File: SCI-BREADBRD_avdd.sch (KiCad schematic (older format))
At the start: 25 parts, among them P8 AVDD, U2 TPS62240DDC, U3 TPS73401DDC, U4 TS5A3159ADCK, U5 TS5A3159ADCK

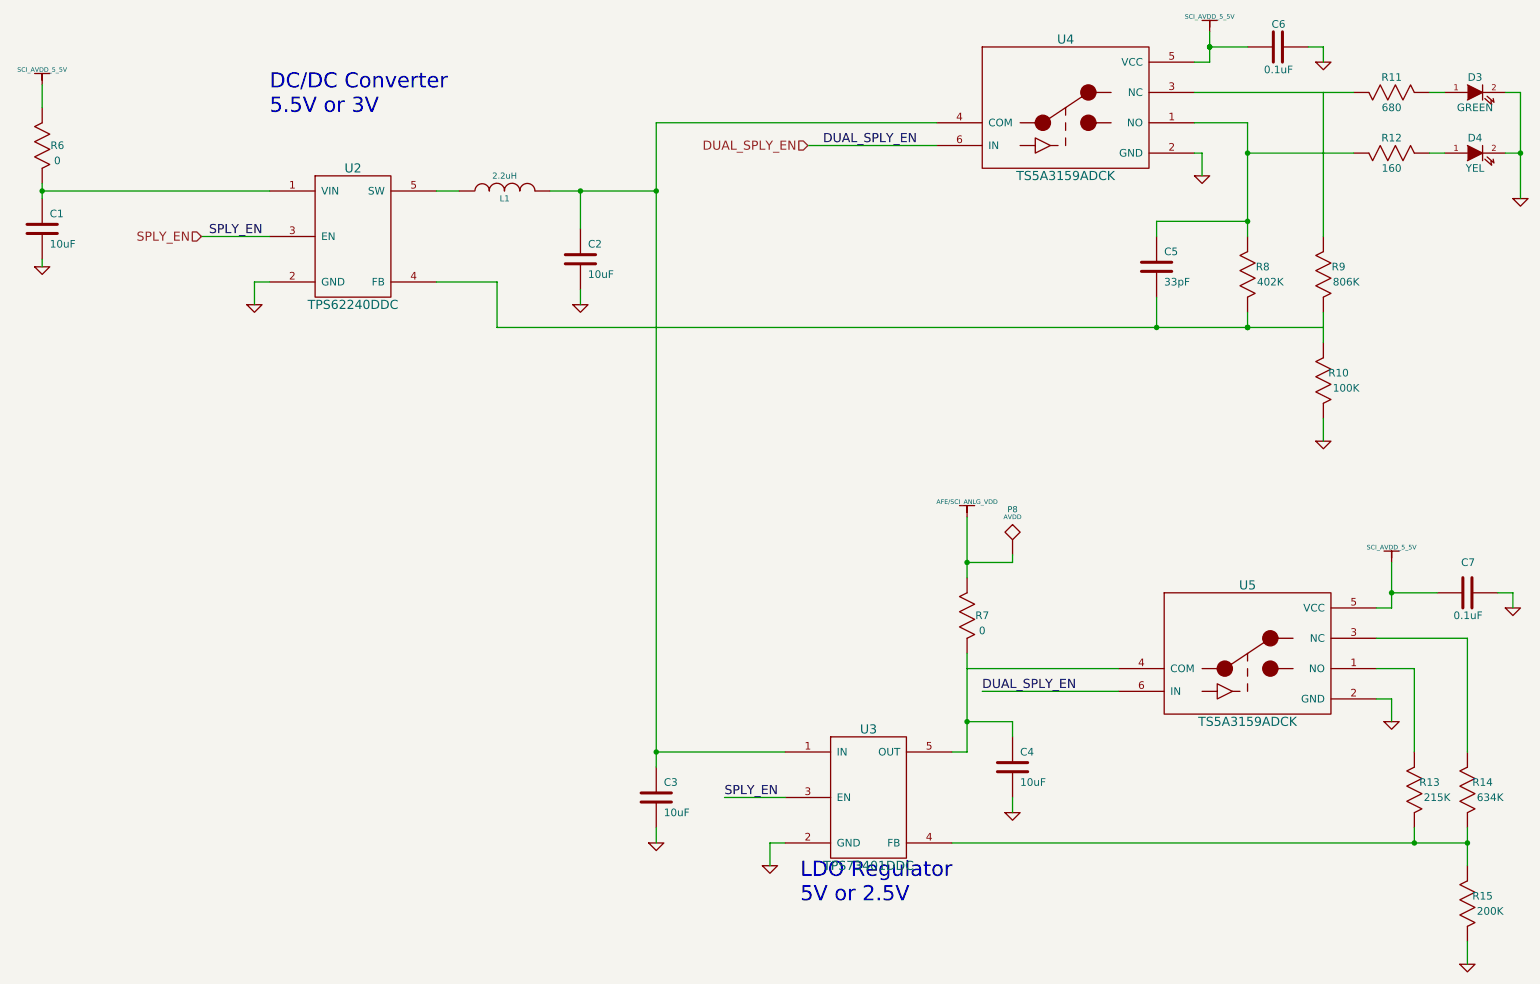
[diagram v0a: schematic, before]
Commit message: Completed ERC. Added some power flags and fixed mis-connected pins.
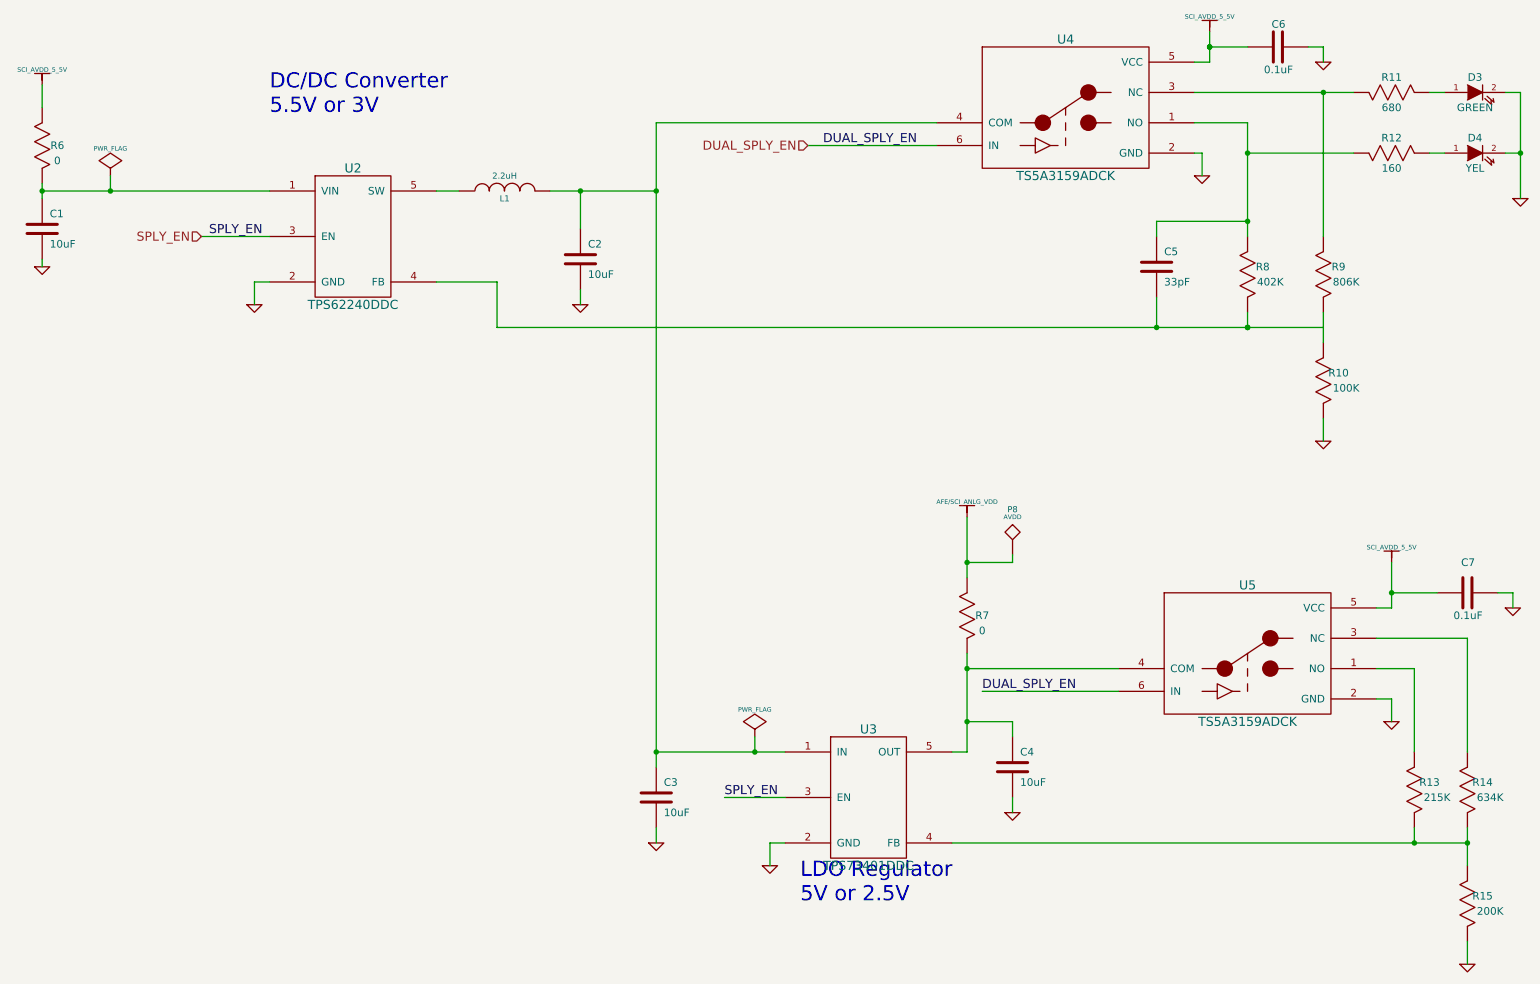
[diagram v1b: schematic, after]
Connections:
- wire segments 70 -> 72
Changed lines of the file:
@@
-EESchema Schematic File Version 2  date Fri 27 Apr 2012 09:11:54 AM EDT
+EESchema Schematic File Version 2  date Fri 27 Apr 2012 11:11:24 AM EDT
 LIBS:custom_transistors
 LIBS:TI_custom
@@
 $EndComp
 $Comp
-L SCI_AVDD_5_5V #PWR046
+L SCI_AVDD_5_5V #PWR050
 U 1 1 4F9A30C2
 P 1000 1150
-F 0 "#PWR046" H 1000 1250 30  0001 C CNN
+F 0 "#PWR050" H 1000 1250 30  0001 C CNN
 F 1 "SCI_AVDD_5_5V" H 1000 1250 30  0000 C CNN
 	1    1000 1150
@@
 $EndComp
 $Comp
-L GND #PWR047
+L GND #PWR051
 U 1 1 4F9A30C8
 P 2400 2600
-F 0 "#PWR047" H 2400 2600 30  0001 C CNN
+F 0 "#PWR051" H 2400 2600 30  0001 C CNN
 F 1 "GND" H 2400 2530 30  0001 C CNN
 	1    2400 2600
@@
 $EndComp
 $Comp
-L GND #PWR048
+L GND #PWR052
 U 1 1 4F9A30D7
 P 1000 2350
-F 0 "#PWR048" H 1000 2350 30  0001 C CNN
+F 0 "#PWR052" H 1000 2350 30  0001 C CNN
 F 1 "GND" H 1000 2280 30  0001 C CNN
 	1    1000 2350
@@
 $EndComp
 $Comp
-L GND #PWR049
+L GND #PWR053
 U 1 1 4F9A30F8
 P 4550 2600
-F 0 "#PWR049" H 4550 2600 30  0001 C CNN
+F 0 "#PWR053" H 4550 2600 30  0001 C CNN
 F 1 "GND" H 4550 2530 30  0001 C CNN
 	1    4550 2600
@@
 $EndComp
 $Comp
-L GND #PWR050
+L GND #PWR054
 U 1 1 4F9A312B
 P 8650 1750
-F 0 "#PWR050" H 8650 1750 30  0001 C CNN
+F 0 "#PWR054" H 8650 1750 30  0001 C CNN
 F 1 "GND" H 8650 1680 30  0001 C CNN
 	1    8650 1750
@@
 $EndComp
 $Comp
-L SCI_AVDD_5_5V #PWR051
+L SCI_AVDD_5_5V #PWR055
 U 1 1 4F9A3131
 P 8700 800
-F 0 "#PWR051" H 8700 900 30  0001 C CNN
+F 0 "#PWR055" H 8700 900 30  0001 C CNN
 F 1 "SCI_AVDD_5_5V" H 8700 900 30  0000 C CNN
 	1    8700 800
@@
 $EndComp
 $Comp
-L GND #PWR052
+L GND #PWR056
 U 1 1 4F9A3140
 P 5800 6300
-F 0 "#PWR052" H 5800 6300 30  0001 C CNN
+F 0 "#PWR056" H 5800 6300 30  0001 C CNN
 F 1 "GND" H 5800 6230 30  0001 C CNN
 	1    5800 6300
@@
 $EndComp
 $Comp
-L SCI_AVDD_5_5V #PWR053
+L SCI_AVDD_5_5V #PWR057
 U 1 1 4F9A3161
 P 9900 4300
-F 0 "#PWR053" H 9900 4400 30  0001 C CNN
+F 0 "#PWR057" H 9900 4400 30  0001 C CNN
 F 1 "SCI_AVDD_5_5V" H 9900 4400 30  0000 C CNN
 	1    9900 4300
@@
 $EndComp
 $Comp
-L GND #PWR054
+L GND #PWR058
 U 1 1 4F9A3167
 P 9900 5350
-F 0 "#PWR054" H 9900 5350 30  0001 C CNN
+F 0 "#PWR058" H 9900 5350 30  0001 C CNN
 F 1 "GND" H 9900 5280 30  0001 C CNN
 	1    9900 5350
@@
 $EndComp
 $Comp
-L GND #PWR055
+L GND #PWR059
 U 1 1 4F9A316D
 P 10400 6950
-F 0 "#PWR055" H 10400 6950 30  0001 C CNN
+F 0 "#PWR059" H 10400 6950 30  0001 C CNN
 F 1 "GND" H 10400 6880 30  0001 C CNN
 	1    10400 6950
@@
 $EndComp
 $Comp
-L GND #PWR056
+L GND #PWR060
 U 1 1 4F9A3173
 P 9450 3500
-F 0 "#PWR056" H 9450 3500 30  0001 C CNN
+F 0 "#PWR060" H 9450 3500 30  0001 C CNN
 F 1 "GND" H 9450 3430 30  0001 C CNN
 	1    9450 3500
@@
 $EndComp
 $Comp
-L GND #PWR057
+L GND #PWR061
 U 1 1 4F9A318D
 P 7400 5950
-F 0 "#PWR057" H 7400 5950 30  0001 C CNN
+F 0 "#PWR061" H 7400 5950 30  0001 C CNN
 F 1 "GND" H 7400 5880 30  0001 C CNN
 	1    7400 5950
@@
 $EndComp
 $Comp
-L GND #PWR058
+L GND #PWR062
 U 1 1 4F9A319C
 P 5050 6150
-F 0 "#PWR058" H 5050 6150 30  0001 C CNN
+F 0 "#PWR062" H 5050 6150 30  0001 C CNN
 F 1 "GND" H 5050 6080 30  0001 C CNN
 	1    5050 6150
@@
 $EndComp
 $Comp
-L AFE/SCI_ANLG_VDD #PWR059
+L AFE/SCI_ANLG_VDD #PWR063
 U 1 1 4F9A31AB
 P 7100 4000
-F 0 "#PWR059" H 7100 4100 30  0001 C CNN
+F 0 "#PWR063" H 7100 4100 30  0001 C CNN
 F 1 "AFE/SCI_ANLG_VDD" H 7100 4100 30  0000 C CNN
 	1    7100 4000
@@
 $EndComp
 $Comp
-L GND #PWR060
+L GND #PWR064
 U 1 1 4F9A5608
 P 10750 1900
-F 0 "#PWR060" H 10750 1900 30  0001 C CNN
+F 0 "#PWR064" H 10750 1900 30  0001 C CNN
 F 1 "GND" H 10750 1830 30  0001 C CNN
 	1    10750 1900
@@
 $EndComp
 $Comp
-L GND #PWR061
+L GND #PWR065
 U 1 1 4F9A573A
 P 10700 4600
-F 0 "#PWR061" H 10700 4600 30  0001 C CNN
+F 0 "#PWR065" H 10700 4600 30  0001 C CNN
 F 1 "GND" H 10700 4530 30  0001 C CNN
 	1    10700 4600
@@
 $EndComp
 $Comp
-L GND #PWR062
+L GND #PWR066
 U 1 1 4F9A5AE1
 P 9450 1000
-F 0 "#PWR062" H 9450 1000 30  0001 C CNN
+F 0 "#PWR066" H 9450 1000 30  0001 C CNN
 F 1 "GND" H 9450 930 30  0001 C CNN
 	1    9450 1000
 	1    0    0    -1
 $EndComp
+$Comp
+L PWR_FLAG #FLG067
+U 1 1 4F9AE62C
+P 5700 5450
+F 0 "#FLG067" H 5700 5545 30  0001 C CNN
+F 1 "PWR_FLAG" H 5700 5630 30  0000 C CNN
+	1    5700 5450
+	1    0    0    -1
+$EndComp
+$Comp
+L PWR_FLAG #FLG068
+U 1 1 4F9AE6F0
+P 1450 1750
+F 0 "#FLG068" H 1450 1845 30  0001 C CNN
+F 1 "PWR_FLAG" H 1450 1930 30  0000 C CNN
+	1    1450 1750
+	1    0    0    -1
+$EndComp
 Wire Wire Line
 	1000 1150 1000 1300
@@
 Wire Wire Line
 	8600 1200 9650 1200
-Wire Wire Line
-	9450 1200 9450 2150
 Wire Wire Line
 	9450 2650 9450 2850
@@
 	7100 4900 7100 5550
 Wire Wire Line
-	7100 5000 8100 5000
-Wire Wire Line
 	9900 5200 9800 5200
 Wire Wire Line
@@
 Wire Wire Line
 	9450 900  9450 1000
+Wire Wire Line
+	9450 2150 9450 1200
+Connection ~ 9450 1200
+Wire Wire Line
+	8100 5000 7100 5000
+Connection ~ 7100 5000
+Wire Wire Line
+	5700 5450 5700 5550
+Connection ~ 5700 5550
+Wire Wire Line
+	1450 1750 1450 1850
+Connection ~ 1450 1850
 $EndSCHEMATC

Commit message: Changed the testpoints to have a refdes of TP? instead of P? and re-annotated.
Fixed a but in better_bom that was causing the last field to be
erroneous.

Added the -e option to better_bom to allow excluding fields
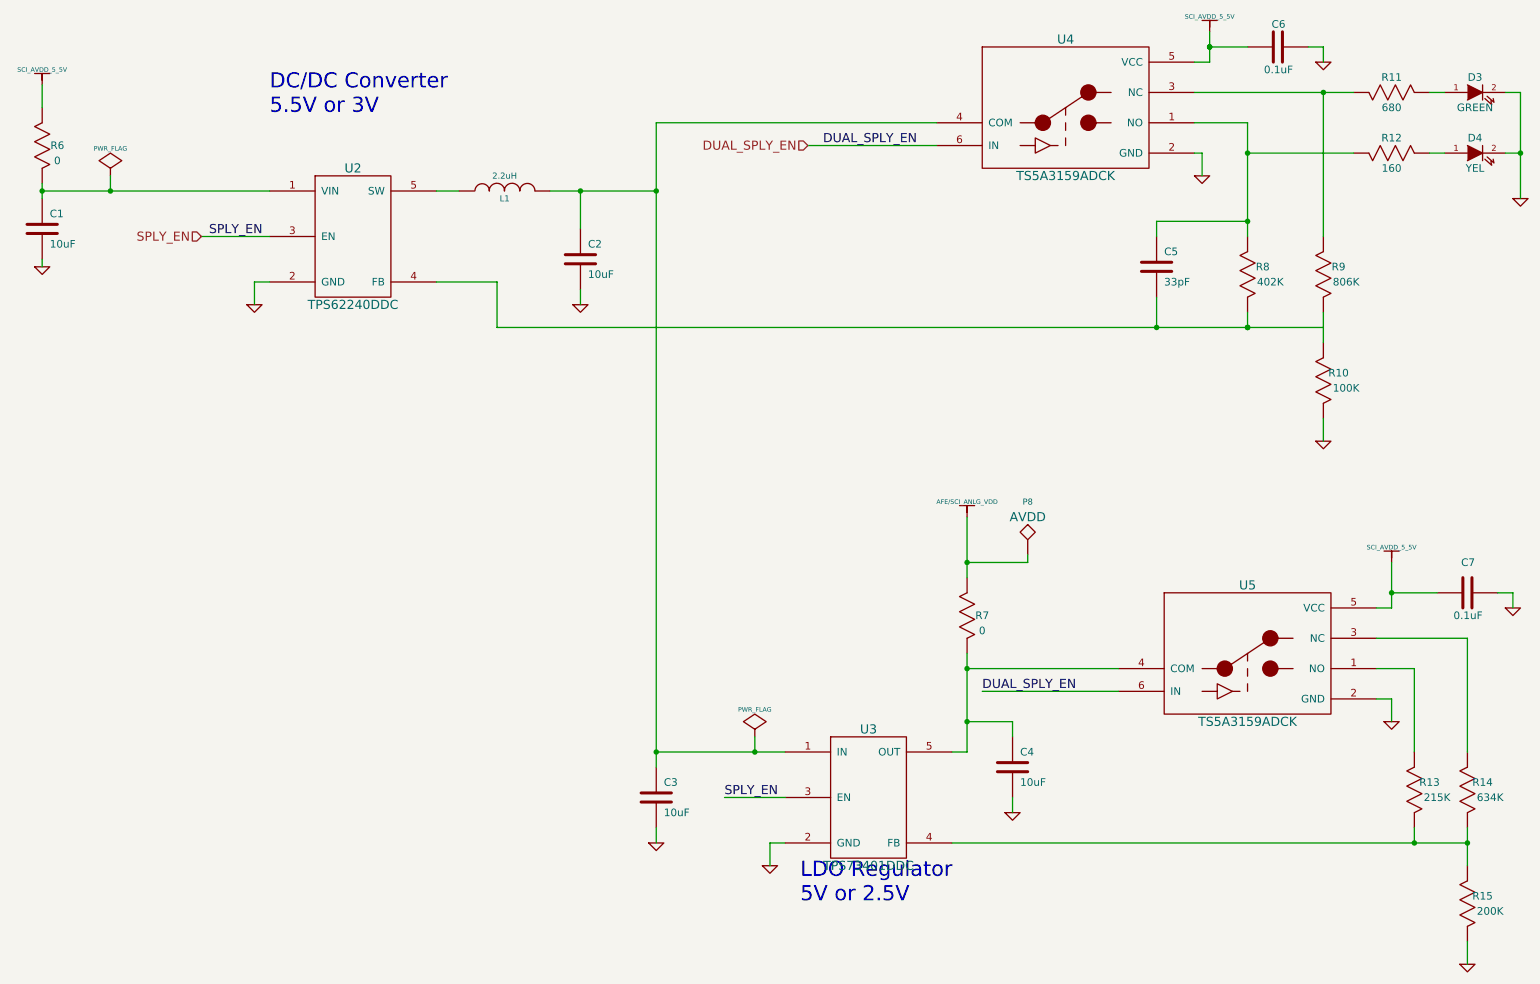
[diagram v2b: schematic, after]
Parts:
- removed P8: AVDD, TESTVIA_p30mil_h20mil, symbol TST
- added P8: TP, TESTVIA_p30mil_h20mil, symbol TP
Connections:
- net AFE/SCI_ANLG_VDD: now also P8.1
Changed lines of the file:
@@
-EESchema Schematic File Version 2  date Fri 27 Apr 2012 11:11:24 AM EDT
+EESchema Schematic File Version 2  date Fri 27 Apr 2012 01:15:52 PM EDT
 LIBS:custom_transistors
 LIBS:TI_custom
@@
 $EndComp
 $Comp
-L SCI_AVDD_5_5V #PWR050
+L SCI_AVDD_5_5V #PWR48
 U 1 1 4F9A30C2
 P 1000 1150
-F 0 "#PWR050" H 1000 1250 30  0001 C CNN
+F 0 "#PWR48" H 1000 1250 30  0001 C CNN
 F 1 "SCI_AVDD_5_5V" H 1000 1250 30  0000 C CNN
 	1    1000 1150
@@
 $EndComp
 $Comp
-L GND #PWR051
+L GND #PWR50
 U 1 1 4F9A30C8
 P 2400 2600
-F 0 "#PWR051" H 2400 2600 30  0001 C CNN
+F 0 "#PWR50" H 2400 2600 30  0001 C CNN
 F 1 "GND" H 2400 2530 30  0001 C CNN
 	1    2400 2600
@@
 $EndComp
 $Comp
-L GND #PWR052
+L GND #PWR49
 U 1 1 4F9A30D7
 P 1000 2350
-F 0 "#PWR052" H 1000 2350 30  0001 C CNN
+F 0 "#PWR49" H 1000 2350 30  0001 C CNN
 F 1 "GND" H 1000 2280 30  0001 C CNN
 	1    1000 2350
@@
 $EndComp
 $Comp
-L GND #PWR053
+L GND #PWR51
 U 1 1 4F9A30F8
 P 4550 2600
-F 0 "#PWR053" H 4550 2600 30  0001 C CNN
+F 0 "#PWR51" H 4550 2600 30  0001 C CNN
 F 1 "GND" H 4550 2530 30  0001 C CNN
 	1    4550 2600
@@
 $EndComp
 $Comp
-L GND #PWR054
+L GND #PWR56
 U 1 1 4F9A312B
 P 8650 1750
-F 0 "#PWR054" H 8650 1750 30  0001 C CNN
+F 0 "#PWR56" H 8650 1750 30  0001 C CNN
 F 1 "GND" H 8650 1680 30  0001 C CNN
 	1    8650 1750
@@
 $EndComp
 $Comp
-L SCI_AVDD_5_5V #PWR055
+L SCI_AVDD_5_5V #PWR57
 U 1 1 4F9A3131
 P 8700 800
-F 0 "#PWR055" H 8700 900 30  0001 C CNN
+F 0 "#PWR57" H 8700 900 30  0001 C CNN
 F 1 "SCI_AVDD_5_5V" H 8700 900 30  0000 C CNN
 	1    8700 800
@@
 $EndComp
 $Comp
-L GND #PWR056
+L GND #PWR53
 U 1 1 4F9A3140
 P 5800 6300
-F 0 "#PWR056" H 5800 6300 30  0001 C CNN
+F 0 "#PWR53" H 5800 6300 30  0001 C CNN
 F 1 "GND" H 5800 6230 30  0001 C CNN
 	1    5800 6300
@@
 $EndComp
 $Comp
-L SCI_AVDD_5_5V #PWR057
+L SCI_AVDD_5_5V #PWR60
 U 1 1 4F9A3161
 P 9900 4300
-F 0 "#PWR057" H 9900 4400 30  0001 C CNN
+F 0 "#PWR60" H 9900 4400 30  0001 C CNN
 F 1 "SCI_AVDD_5_5V" H 9900 4400 30  0000 C CNN
 	1    9900 4300
@@
 $EndComp
 $Comp
-L GND #PWR058
+L GND #PWR61
 U 1 1 4F9A3167
 P 9900 5350
-F 0 "#PWR058" H 9900 5350 30  0001 C CNN
+F 0 "#PWR61" H 9900 5350 30  0001 C CNN
 F 1 "GND" H 9900 5280 30  0001 C CNN
 	1    9900 5350
@@
 $EndComp
 $Comp
-L GND #PWR059
+L GND #PWR62
 U 1 1 4F9A316D
 P 10400 6950
-F 0 "#PWR059" H 10400 6950 30  0001 C CNN
+F 0 "#PWR62" H 10400 6950 30  0001 C CNN
 F 1 "GND" H 10400 6880 30  0001 C CNN
 	1    10400 6950
@@
 $EndComp
 $Comp
-L GND #PWR060
+L GND #PWR59
 U 1 1 4F9A3173
 P 9450 3500
-F 0 "#PWR060" H 9450 3500 30  0001 C CNN
+F 0 "#PWR59" H 9450 3500 30  0001 C CNN
 F 1 "GND" H 9450 3430 30  0001 C CNN
 	1    9450 3500
@@
 $EndComp
 $Comp
-L GND #PWR061
+L GND #PWR55
 U 1 1 4F9A318D
 P 7400 5950
-F 0 "#PWR061" H 7400 5950 30  0001 C CNN
+F 0 "#PWR55" H 7400 5950 30  0001 C CNN
 F 1 "GND" H 7400 5880 30  0001 C CNN
 	1    7400 5950
@@
 $EndComp
 $Comp
-L GND #PWR062
+L GND #PWR52
 U 1 1 4F9A319C
 P 5050 6150
-F 0 "#PWR062" H 5050 6150 30  0001 C CNN
+F 0 "#PWR52" H 5050 6150 30  0001 C CNN
 F 1 "GND" H 5050 6080 30  0001 C CNN
 	1    5050 6150
@@
 $EndComp
 $Comp
-L AFE/SCI_ANLG_VDD #PWR063
+L AFE/SCI_ANLG_VDD #PWR54
 U 1 1 4F9A31AB
 P 7100 4000
-F 0 "#PWR063" H 7100 4100 30  0001 C CNN
+F 0 "#PWR54" H 7100 4100 30  0001 C CNN
 F 1 "AFE/SCI_ANLG_VDD" H 7100 4100 30  0000 C CNN
 	1    7100 4000
-	1    0    0    -1
-$EndComp
-$Comp
-L TST P8
-U 1 1 4F9A31B3
-P 7400 4250
-F 0 "P8" H 7400 4550 40  0000 C CNN
-F 1 "AVDD" H 7400 4500 30  0000 C CNN
-F 2 "TESTVIA_p30mil_h20mil" H 7400 4250 60  0001 C CNN
-F 4 "TESTPOINT VIA" H 7400 4250 60  0001 C CNN "Description"
-F 5 "NO PART. TEST PAD ONLY." H 7400 4250 60  0001 C CNN "Note"
-	1    7400 4250
 	1    0    0    -1
 $EndComp
@@
 $EndComp
 $Comp
-L GND #PWR064
+L GND #PWR64
 U 1 1 4F9A5608
 P 10750 1900
-F 0 "#PWR064" H 10750 1900 30  0001 C CNN
+F 0 "#PWR64" H 10750 1900 30  0001 C CNN
 F 1 "GND" H 10750 1830 30  0001 C CNN
 	1    10750 1900
@@
 $EndComp
 $Comp
-L GND #PWR065
+L GND #PWR63
 U 1 1 4F9A573A
 P 10700 4600
-F 0 "#PWR065" H 10700 4600 30  0001 C CNN
+F 0 "#PWR63" H 10700 4600 30  0001 C CNN
 F 1 "GND" H 10700 4530 30  0001 C CNN
 	1    10700 4600
@@
 $EndComp
 $Comp
-L GND #PWR066
+L GND #PWR58
 U 1 1 4F9A5AE1
 P 9450 1000
-F 0 "#PWR066" H 9450 1000 30  0001 C CNN
+F 0 "#PWR58" H 9450 1000 30  0001 C CNN
 F 1 "GND" H 9450 930 30  0001 C CNN
 	1    9450 1000
@@
 $EndComp
 $Comp
-L PWR_FLAG #FLG067
+L PWR_FLAG #FLG4
 U 1 1 4F9AE62C
 P 5700 5450
-F 0 "#FLG067" H 5700 5545 30  0001 C CNN
+F 0 "#FLG4" H 5700 5545 30  0001 C CNN
 F 1 "PWR_FLAG" H 5700 5630 30  0000 C CNN
 	1    5700 5450
@@
 $EndComp
 $Comp
-L PWR_FLAG #FLG068
+L PWR_FLAG #FLG3
 U 1 1 4F9AE6F0
 P 1450 1750
-F 0 "#FLG068" H 1450 1845 30  0001 C CNN
+F 0 "#FLG3" H 1450 1845 30  0001 C CNN
 F 1 "PWR_FLAG" H 1450 1930 30  0000 C CNN
 	1    1450 1750
@@
 	1000 1150 1000 1300
 Wire Wire Line
-	1000 1850 2500 1850
+	1000 1850 1450 1850
+Wire Wire Line
+	1450 1850 2500 1850
 Wire Wire Line
 	2400 2600 2400 2450
@@
 	2400 2450 2500 2450
 Wire Wire Line
-	1000 1800 1000 1900
+	1000 1800 1000 1850
+Wire Wire Line
+	1000 1850 1000 1900
 Connection ~ 1000 1850
 Wire Wire Line
@@
 	3600 1850 3750 1850
 Wire Wire Line
-	4350 1850 5050 1850
+	4350 1850 4550 1850
+Wire Wire Line
+	4550 1850 5050 1850
 Wire Wire Line
 	4550 2600 4550 2500
@@
 	8600 1400 8950 1400
 Wire Wire Line
-	8950 1400 8950 2150
+	8950 1400 8950 1600
+Wire Wire Line
+	8950 1600 8950 2050
+Wire Wire Line
+	8950 2050 8950 2150
 Wire Wire Line
 	8650 1600 8650 1750
@@
 	8650 1600 8600 1600
 Wire Wire Line
-	8600 1200 9650 1200
+	8600 1200 9450 1200
+Wire Wire Line
+	9450 1200 9650 1200
 Wire Wire Line
 	9450 2650 9450 2850
 Wire Wire Line
-	4000 2750 9450 2750
+	4000 2750 8350 2750
+Wire Wire Line
+	8350 2750 8950 2750
+Wire Wire Line
+	8950 2750 9450 2750
 Connection ~ 8950 2750
 Connection ~ 8950 2750
@@
 	4000 2450 3600 2450
 Wire Wire Line
-	8700 800  8700 1000
+	8700 800  8700 900
+Wire Wire Line
+	8700 900  8700 1000
 Wire Wire Line
 	8700 1000 8600 1000
@@
 	7100 5550 7000 5550
 Wire Wire Line
-	7100 4900 7100 5550
+	7100 4900 7100 5000
+Wire Wire Line
+	7100 5000 7100 5350
+Wire Wire Line
+	7100 5350 7100 5550
 Wire Wire Line
 	9900 5200 9800 5200
@@
 	10050 5000 9800 5000
 Wire Wire Line
-	10400 6050 10400 6300
+	10400 6050 10400 6150
+Wire Wire Line
+	10400 6150 10400 6300
 Wire Wire Line
 	10050 6050 10050 6150
 Wire Wire Line
-	7000 6150 10400 6150
+	7000 6150 10050 6150
+Wire Wire Line
+	10050 6150 10400 6150
 Connection ~ 10400 6150
 Connection ~ 10050 6150
@@
 	5050 6150 5050 6050
 Wire Wire Line
-	7100 4000 7100 4400
-Wire Wire Line
-	7100 4300 7400 4300
-Wire Wire Line
-	7400 4300 7400 4250
+	7100 4000 7100 4300
+Wire Wire Line
+	7100 4300 7100 4400
+Wire Wire Line
+	7100 4300 7500 4300
+Wire Wire Line
+	7500 4300 7500 4250
 Connection ~ 7100 4300
 Wire Wire Line
@@
 	6050 1550 6900 1550
 Wire Wire Line
-	5050 1400 5050 5650
+	5050 1400 5050 1850
+Wire Wire Line
+	5050 1850 5050 5550
+Wire Wire Line
+	5050 5550 5050 5650
 Wire Wire Line
 	4550 2100 4550 1850
 Connection ~ 4550 1850
 Wire Wire Line
-	5050 5550 5900 5550
+	5050 5550 5700 5550
+Wire Wire Line
+	5700 5550 5900 5550
 Connection ~ 5050 1850
 Connection ~ 5050 5550
@@
 Connection ~ 8950 1600
 Wire Wire Line
-	10750 1200 10750 1900
+	10750 1200 10750 1600
+Wire Wire Line
+	10750 1600 10750 1900
 Connection ~ 10750 1600
 Wire Wire Line
@@
 	10700 4500 10700 4600
 Wire Wire Line
-	9900 4300 9900 4600
+	9900 4300 9900 4500
+Wire Wire Line
+	9900 4500 9900 4600
 Wire Wire Line
 	9900 4600 9800 4600
@@
 	1450 1750 1450 1850
 Connection ~ 1450 1850
+$Comp
+L TP P8
+U 1 1 4F9AD783
+P 7500 4250
+F 0 "P8" H 7500 4600 40  0000 C CNN
+F 1 "TP" H 7500 4500 30  0001 C CNN
+F 2 "TESTVIA_p30mil_h20mil" H 7500 4250 60  0001 C CNN
+F 4 "TESTPOINT VIA" H 7500 4250 60  0001 C CNN "Description"
+F 5 "NO PART. TEST PAD ONLY." H 7500 4250 60  0001 C CNN "Note"
+F 6 "AVDD" H 7500 4500 60  0000 C CNN "Silkscreen"
+	1    7500 4250
+	1    0    0    -1
+$EndComp
 $EndSCHEMATC
